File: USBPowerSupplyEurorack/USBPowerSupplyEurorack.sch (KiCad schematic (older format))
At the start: 9 parts, among them J1 1734366-1, T1 RS6-0512D

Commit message: changed diode for lower forward voltage, prepared 2HP PCB contour
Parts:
- removed D1: SS36, SS36:DIOM8059X265N, symbol SS36:SS36
- added C?: 100nF close to Switch, symbol Device:CP_Small
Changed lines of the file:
@@
 $EndDescr
-$Comp
-L SS36:SS36 D1
-U 1 1 5FE03083
-P 2330 1470
-F 0 "D1" H 2730 1203 50  0000 C CNN
-F 1 "SS36" H 2730 1294 50  0000 C CNN
-F 2 "SS36:DIOM8059X265N" H 2830 1620 50  0001 L CNN
-F 3 "http://www.onsemi.com/pub/Collateral/SS39-D.PDF" H 2830 1520 50  0001 L CNN
-F 4 "ON SEMICONDUCTOR - SS36 - DIODE, SCHOTTKY, 3A, 60V, DO-214AB-3" H 2830 1420 50  0001 L CNN "Description"
-F 5 "2.65" H 2830 1320 50  0001 L CNN "Height"
-F 6 "ON Semiconductor" H 2830 1220 50  0001 L CNN "Manufacturer_Name"
-F 7 "SS36" H 2830 1120 50  0001 L CNN "Manufacturer_Part_Number"
-F 8 "SS36" H 2830 1020 50  0001 L CNN "Arrow Part Number"
-F 9 "https://www.arrow.com/en/products/ss36/on-semiconductor" H 2830 920 50  0001 L CNN "Arrow Price/Stock"
-F 10 "512-SS36" H 2830 820 50  0001 L CNN "Mouser Part Number"
-F 11 "https://www.mouser.co.uk/ProductDetail/ON-Semiconductor-Fairchild/SS36/?qs=3wuez3jz59JyNj1can%252BtMw%3D%3D" H 2830 720 50  0001 L CNN "Mouser Price/Stock"
-	1    2330 1470
-	-1   0    0    1
-$EndComp
 $Comp
 L Device:CP1_Small C1
@@
 NoConn ~ 1510 1670
 $Comp
+L Device:CP1_Small C?
+U 1 1 5FE2664F
+P 6420 5130
+F 0 "C?" H 6511 5176 50  0000 L CNN
+F 1 "22uF" H 6511 5085 50  0000 L CNN
+F 2 "" H 6420 5130 50  0001 C CNN
+F 3 "~" H 6420 5130 50  0001 C CNN
+	1    6420 5130
+	1    0    0    -1
+$EndComp
+Wire Wire Line
+	6420 5230 6420 5420
+Wire Wire Line
+	6420 5030 6420 4840
+Wire Wire Line
+	6010 4970 6010 4840
+Wire Wire Line
+	6010 4840 6420 4840
+Connection ~ 6420 4840
+Wire Wire Line
+	6010 5270 6010 5420
+Wire Wire Line
+	6010 5420 6420 5420
+Connection ~ 6420 5420
+Wire Wire Line
+	5630 5020 5630 4840
+Wire Wire Line
+	5630 4840 6010 4840
+Connection ~ 6010 4840
+Wire Wire Line
+	5630 5220 5630 5420
+Wire Wire Line
+	5630 5420 6010 5420
+Connection ~ 6010 5420
+$Comp
+L power:GND #PWR?
+U 1 1 5FE34916
+P 5630 5520
+F 0 "#PWR?" H 5630 5270 50  0001 C CNN
+F 1 "GND" H 5635 5347 50  0000 C CNN
+F 2 "" H 5630 5520 50  0001 C CNN
+F 3 "" H 5630 5520 50  0001 C CNN
+	1    5630 5520
+	1    0    0    -1
+$EndComp
+Wire Wire Line
+	5630 5520 5630 5420
+Connection ~ 5630 5420
+Wire Wire Line
+	2230 1470 2310 1470
+Wire Wire Line
+	2310 1470 2310 1420
+Wire Wire Line
+	5630 4740 5630 4840
+Connection ~ 5630 4840
+Text GLabel 9120 4870 2    50   Input ~ 0
++Vin
+Text GLabel 9400 5180 2    50   Input ~ 0
+-Vin
+Wire Wire Line
+	6830 4840 6830 5090
+Wire Wire Line
+	6420 4840 6830 4840
+Wire Wire Line
+	6830 5420 6830 5190
+Wire Wire Line
+	6420 5420 6830 5420
+$Comp
 L 744235601:744235601 L?
 U 1 1 5FE25D51
@@
 $EndComp
 $Comp
-L Device:CP1_Small C?
-U 1 1 5FE2664F
-P 6420 5130
-F 0 "C?" H 6511 5176 50  0000 L CNN
-F 1 "22uF" H 6511 5085 50  0000 L CNN
-F 2 "" H 6420 5130 50  0001 C CNN
-F 3 "~" H 6420 5130 50  0001 C CNN
-	1    6420 5130
-	1    0    0    -1
-$EndComp
-Wire Wire Line
-	6420 5230 6420 5420
-Wire Wire Line
-	6420 5420 6830 5420
-Wire Wire Line
-	6830 5420 6830 5190
-Wire Wire Line
-	6420 5030 6420 4840
-Wire Wire Line
-	6420 4840 6830 4840
-Wire Wire Line
-	6830 4840 6830 5090
-Wire Wire Line
-	6010 4970 6010 4840
-Wire Wire Line
-	6010 4840 6420 4840
-Connection ~ 6420 4840
-Wire Wire Line
-	6010 5270 6010 5420
-Wire Wire Line
-	6010 5420 6420 5420
-Connection ~ 6420 5420
-Wire Wire Line
-	5630 5020 5630 4840
-Wire Wire Line
-	5630 4840 6010 4840
-Connection ~ 6010 4840
-Wire Wire Line
-	5630 5220 5630 5420
-Wire Wire Line
-	5630 5420 6010 5420
-Connection ~ 6010 5420
-$Comp
-L power:GND #PWR?
-U 1 1 5FE34916
-P 5630 5520
-F 0 "#PWR?" H 5630 5270 50  0001 C CNN
-F 1 "GND" H 5635 5347 50  0000 C CNN
-F 2 "" H 5630 5520 50  0001 C CNN
-F 3 "" H 5630 5520 50  0001 C CNN
-	1    5630 5520
-	1    0    0    -1
-$EndComp
-Wire Wire Line
-	5630 5520 5630 5420
-Connection ~ 5630 5420
-Text GLabel 7630 5190 2    50   Input ~ 0
--Vin
-Text GLabel 7630 5090 2    50   Input ~ 0
-+Vin
-Wire Wire Line
-	2230 1470 2310 1470
-Wire Wire Line
-	2310 1470 2310 1420
-Wire Wire Line
-	5630 4740 5630 4840
-Connection ~ 5630 4840
+L Device:CP_Small C?
+U 1 1 5FE49BEB
+P 8000 5130
+F 0 "C?" H 8088 5176 50  0000 L CNN
+F 1 "100nF close to Switch" H 8088 5085 50  0000 L CNN
+F 2 "" H 8000 5130 50  0001 C CNN
+F 3 "~" H 8000 5130 50  0001 C CNN
+	1    8000 5130
+	1    0    0    -1
+$EndComp
 $EndSCHEMATC

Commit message: completed schematics
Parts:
- added C4: 100nF MLCC, symbol Device:CP_Small
- added C5, C6: 1uF, symbol Device:CP1_Small
- added C7: 47uF, symbol Device:CP1_Small
- added D1: LSM115JE3_TR13, DIOM5436X330N, symbol LSM115JE3_TR13:LSM115JE3_TR13
- added D3, D4: 1N4004, Diode_THT:D_DO-41_SOD81_P10.16mm_Horizontal, symbol Diode:1N4004
- added J2: EURO_PWR_2x5, symbol eurocad:EURO_PWR_2x5
- C2: renamed from C?; value 22uF -> 22uFMLCC
- C3: renamed from C?; value 100nF close to Switch -> 100nF MLCC
- gave numbers to parts that had none: 2
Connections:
- net labels added: COM
- wire segments 26 -> 59
- no-connect marks 4 -> 5
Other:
- note added: "DC-DC switching regulator"
- note added: "Output connector"
- note added: "Output filtering"
- note added: "Pre-regulator filtering and surge protection"
- moved on the sheet: C1, C2, C3, D2, J1, L1, R1, S1

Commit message: finished schematics, added PMOS for reversed polarity protection
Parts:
- removed D1: LSM115JE3_TR13, DIOM5436X330N, symbol LSM115JE3_TR13:LSM115JE3_TR13
- added F1: 1812L110_16DR, FUSC4632X125N, symbol 1812L110_16DR:1812L110_16DR
- added Q1: Q_PMOS_GSD, digikey-footprints:SOT-23-3, symbol Device:Q_PMOS_GSD
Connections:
- wire segments 59 -> 66
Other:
- note added: "Pre-regulator filtering and surge/reversed polarity protection"
- note removed: "Pre-regulator filtering and surge protection"
- moved on the sheet: C1, C2, C3, C4, C5, C6, C7, D2, D3, D4, J1, J2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

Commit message: finished schematics
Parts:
- removed T1: RS6-0512D, RS6-0512D:RS60505S, symbol RS6-0512D:RS6-0512D
- added PS? (x2): RS6-0512S, RS6-0512S:RS60512S, symbol RS6-0512S:RS6-0512S
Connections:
- net labels added: +12, -12, 0V
- wire segments 66 -> 68
- no-connect marks 5 -> 8
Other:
- note added: "DC-DC switching regulators"
- note removed: "DC-DC switching regulator"
- moved on the sheet: C3, C4, C5, C6, D3, D4, J2

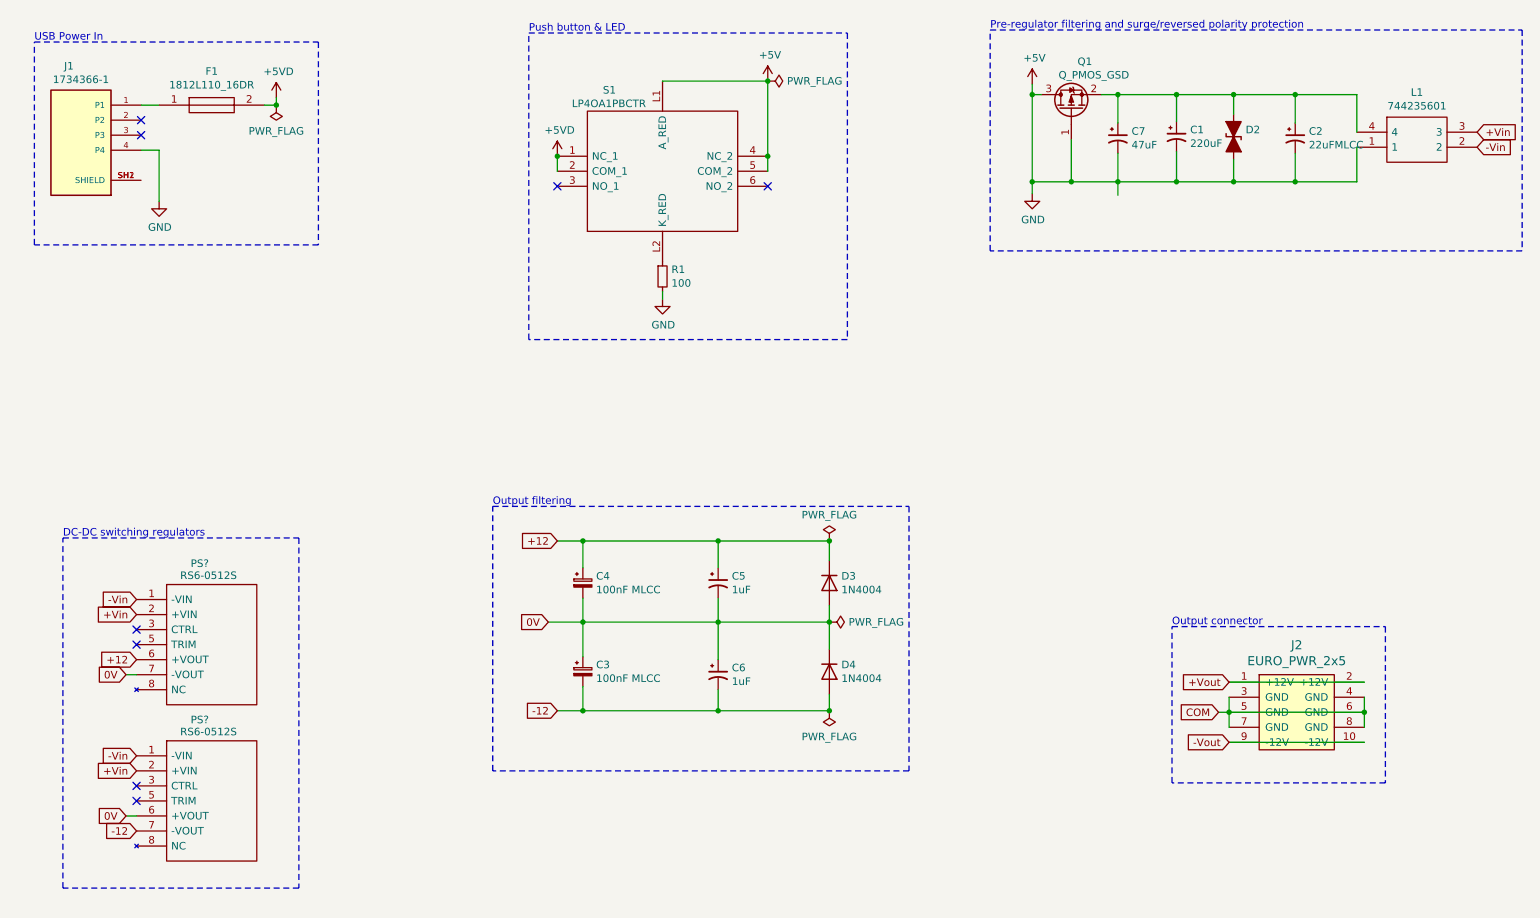
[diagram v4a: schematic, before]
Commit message: replaced power plug with open one
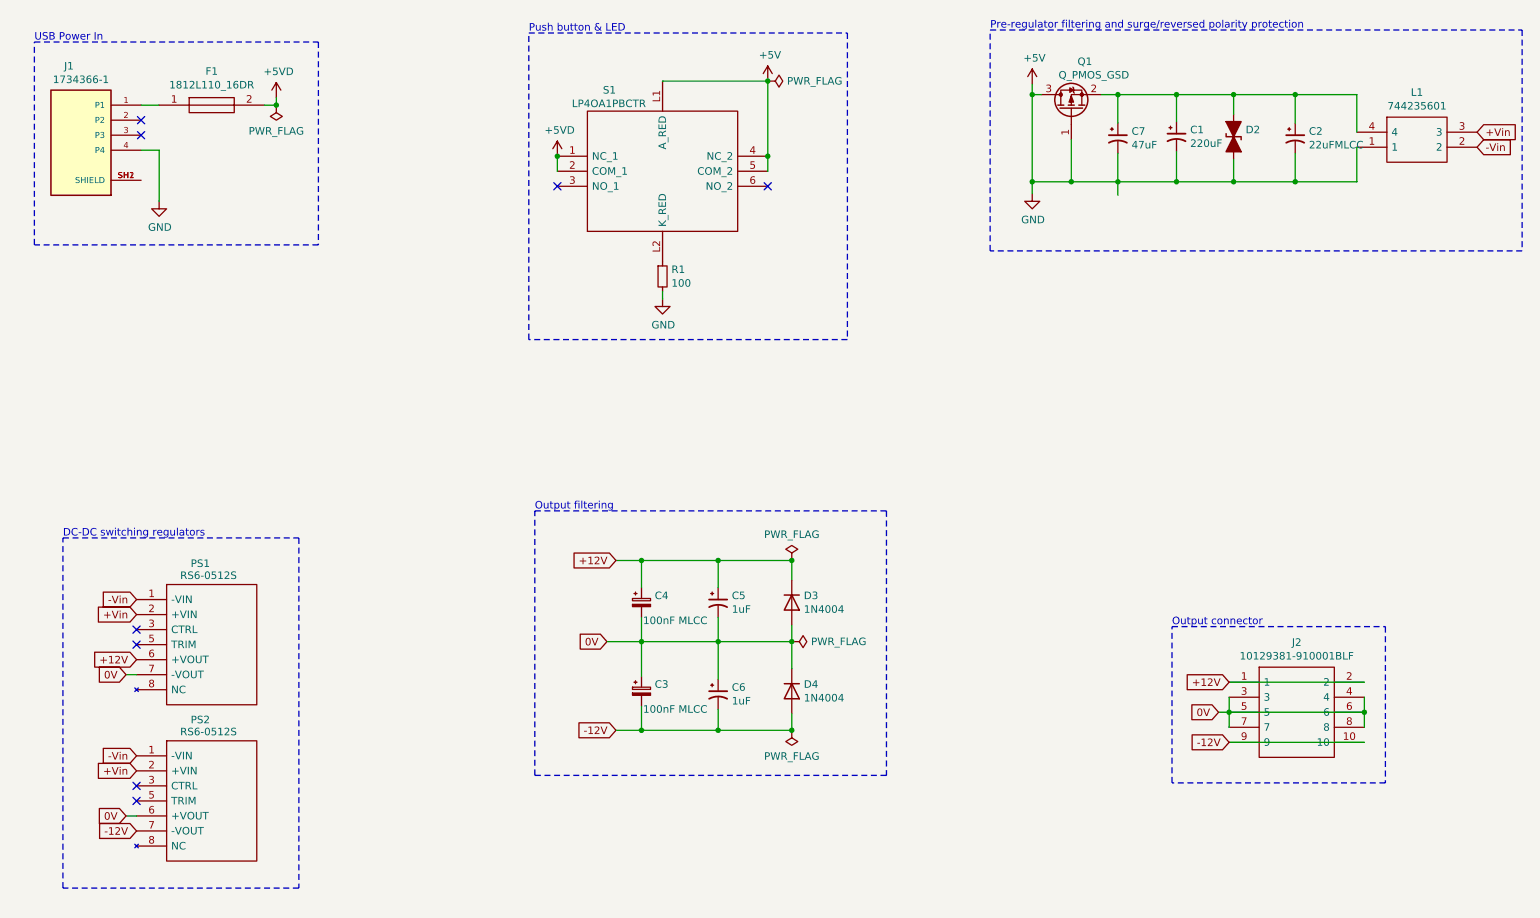
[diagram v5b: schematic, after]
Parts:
- removed J2: EURO_PWR_2x5, symbol eurocad:EURO_PWR_2x5
- added J2: 10129381-910001BLF, HDRV10W67P254_2X5_1270X483X858P, symbol 10129381-910001BLF:10129381-910001BLF
- gave numbers to parts that had none: 2
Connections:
- net 0V: now also J2.3, J2.4, J2.5, J2.6, J2.7, J2.8
- net +12 renamed +12V
- net +12V: now also J2.1, J2.2
- net -12 renamed -12V
- net -12V: now also J2.10, J2.9
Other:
- moved on the sheet: C3, C4, C5, C6, D3, D4
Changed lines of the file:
@@
 L Device:CP_Small C3
 U 1 1 5FE49BEB
-P 4600 5260
-F 0 "C3" H 4688 5306 50  0000 L CNN
-F 1 "100nF MLCC" H 4688 5215 50  0000 L CNN
-F 2 "" H 4600 5260 50  0001 C CNN
-F 3 "~" H 4600 5260 50  0001 C CNN
-	1    4600 5260
+P 4990 5390
+F 0 "C3" H 5078 5436 50  0000 L CNN
+F 1 "100nF MLCC" H 5000 5270 50  0000 L CNN
+F 2 "" H 4990 5390 50  0001 C CNN
+F 3 "~" H 4990 5390 50  0001 C CNN
+	1    4990 5390
 	1    0    0    -1
 $EndComp
@@
 $EndComp
 Wire Wire Line
-	4600 5360 4600 5520
-Wire Wire Line
-	4600 5520 4430 5520
+	4990 5490 4990 5650
+Wire Wire Line
+	4990 5650 4820 5650
 Wire Wire Line
 	8550 1420 8160 1420
@@
 L Diode:1N4004 D3
 U 1 1 5FE6DCB8
-P 6240 4670
-F 0 "D3" V 6194 4750 50  0000 L CNN
-F 1 "1N4004" V 6285 4750 50  0000 L CNN
-F 2 "Diode_THT:D_DO-41_SOD81_P10.16mm_Horizontal" H 6240 4495 50  0001 C CNN
-F 3 "http://www.vishay.com/docs/88503/1n4001.pdf" H 6240 4670 50  0001 C CNN
-	1    6240 4670
+P 5990 4800
+F 0 "D3" V 5944 4880 50  0000 L CNN
+F 1 "1N4004" V 6035 4880 50  0000 L CNN
+F 2 "Diode_THT:D_DO-41_SOD81_P10.16mm_Horizontal" H 5990 4625 50  0001 C CNN
+F 3 "http://www.vishay.com/docs/88503/1n4001.pdf" H 5990 4800 50  0001 C CNN
+	1    5990 4800
 	0    1    1    0
 $EndComp
@@
 L Device:CP_Small C4
 U 1 1 5FE6E630
-P 4600 4670
-F 0 "C4" H 4688 4716 50  0000 L CNN
-F 1 "100nF MLCC" H 4688 4625 50  0000 L CNN
-F 2 "" H 4600 4670 50  0001 C CNN
-F 3 "~" H 4600 4670 50  0001 C CNN
-	1    4600 4670
-	1    0    0    -1
-$EndComp
-Wire Wire Line
-	4430 4390 4600 4390
-Wire Wire Line
-	4600 4390 4600 4570
-Wire Wire Line
-	4600 4770 4600 4930
-Wire Wire Line
-	4600 4930 4370 4930
-Wire Wire Line
-	4600 5160 4600 4930
-Connection ~ 4600 4930
+P 4990 4800
+F 0 "C4" H 5078 4846 50  0000 L CNN
+F 1 "100nF MLCC" H 5000 4680 50  0000 L CNN
+F 2 "" H 4990 4800 50  0001 C CNN
+F 3 "~" H 4990 4800 50  0001 C CNN
+	1    4990 4800
+	1    0    0    -1
+$EndComp
+Wire Wire Line
+	4820 4520 4990 4520
+Wire Wire Line
+	4990 4520 4990 4700
+Wire Wire Line
+	4990 4900 4990 5060
+Wire Wire Line
+	4990 5060 4760 5060
+Wire Wire Line
+	4990 5290 4990 5060
+Connection ~ 4990 5060
 $Comp
 L Device:CP1_Small C5
 U 1 1 5FE73D6E
-P 5500 4670
-F 0 "C5" H 5591 4716 50  0000 L CNN
-F 1 "1uF" H 5591 4625 50  0000 L CNN
-F 2 "" H 5500 4670 50  0001 C CNN
-F 3 "~" H 5500 4670 50  0001 C CNN
-	1    5500 4670
+P 5500 4800
+F 0 "C5" H 5591 4846 50  0000 L CNN
+F 1 "1uF" H 5591 4755 50  0000 L CNN
+F 2 "" H 5500 4800 50  0001 C CNN
+F 3 "~" H 5500 4800 50  0001 C CNN
+	1    5500 4800
 	1    0    0    -1
 $EndComp
@@
 L Device:CP1_Small C6
 U 1 1 5FE74A1F
-P 5500 5280
-F 0 "C6" H 5591 5326 50  0000 L CNN
-F 1 "1uF" H 5591 5235 50  0000 L CNN
-F 2 "" H 5500 5280 50  0001 C CNN
-F 3 "~" H 5500 5280 50  0001 C CNN
-	1    5500 5280
-	1    0    0    -1
-$EndComp
-Wire Wire Line
-	4600 4390 5500 4390
-Wire Wire Line
-	5500 4390 5500 4570
-Connection ~ 4600 4390
-Wire Wire Line
-	5500 4770 5500 4930
-Wire Wire Line
-	5500 5380 5500 5520
-Wire Wire Line
-	5500 5520 4600 5520
-Connection ~ 4600 5520
-Wire Wire Line
-	4600 4930 5500 4930
-Connection ~ 5500 4930
-Wire Wire Line
-	5500 4930 5500 5180
+P 5500 5410
+F 0 "C6" H 5591 5456 50  0000 L CNN
+F 1 "1uF" H 5591 5365 50  0000 L CNN
+F 2 "" H 5500 5410 50  0001 C CNN
+F 3 "~" H 5500 5410 50  0001 C CNN
+	1    5500 5410
+	1    0    0    -1
+$EndComp
+Wire Wire Line
+	4990 4520 5500 4520
+Wire Wire Line
+	5500 4520 5500 4700
+Connection ~ 4990 4520
+Wire Wire Line
+	5500 4900 5500 5060
+Wire Wire Line
+	5500 5510 5500 5650
+Wire Wire Line
+	5500 5650 4990 5650
+Connection ~ 4990 5650
+Wire Wire Line
+	4990 5060 5500 5060
+Connection ~ 5500 5060
+Wire Wire Line
+	5500 5060 5500 5310
 $Comp
 L Diode:1N4004 D4
 U 1 1 5FE81B4A
-P 6240 5260
-F 0 "D4" V 6194 5340 50  0000 L CNN
-F 1 "1N4004" V 6285 5340 50  0000 L CNN
-F 2 "Diode_THT:D_DO-41_SOD81_P10.16mm_Horizontal" H 6240 5085 50  0001 C CNN
-F 3 "http://www.vishay.com/docs/88503/1n4001.pdf" H 6240 5260 50  0001 C CNN
-	1    6240 5260
+P 5990 5390
+F 0 "D4" V 5944 5470 50  0000 L CNN
+F 1 "1N4004" V 6035 5470 50  0000 L CNN
+F 2 "Diode_THT:D_DO-41_SOD81_P10.16mm_Horizontal" H 5990 5215 50  0001 C CNN
+F 3 "http://www.vishay.com/docs/88503/1n4001.pdf" H 5990 5390 50  0001 C CNN
+	1    5990 5390
 	0    1    1    0
 $EndComp
 Wire Wire Line
-	5500 5520 6240 5520
-Wire Wire Line
-	6240 5520 6240 5410
-Connection ~ 5500 5520
-Wire Wire Line
-	5500 4930 6240 4930
-Wire Wire Line
-	6240 4820 6240 4930
-Connection ~ 6240 4930
-Wire Wire Line
-	6240 4930 6240 5110
-Wire Wire Line
-	6240 4520 6240 4390
-Wire Wire Line
-	6240 4390 5500 4390
-Connection ~ 5500 4390
+	5500 5650 5990 5650
+Wire Wire Line
+	5990 5650 5990 5540
+Connection ~ 5500 5650
+Wire Wire Line
+	5500 5060 5990 5060
+Wire Wire Line
+	5990 4950 5990 5060
+Connection ~ 5990 5060
+Wire Wire Line
+	5990 5060 5990 5240
+Wire Wire Line
+	5990 4650 5990 4520
+Wire Wire Line
+	5990 4520 5500 4520
+Connection ~ 5500 4520
 Wire Notes Line
 	1140 4370 2710 4370
@@
 Text Notes 1140 4370 0    50   ~ 0
 DC-DC switching regulators
-$Comp
-L eurocad:EURO_PWR_2x5 J2
-U 1 1 5FE9238E
-P 9350 5530
-F 0 "J2" H 9350 5977 60  0000 C CNN
-F 1 "EURO_PWR_2x5" H 9350 5871 60  0000 C CNN
-F 2 "" H 9350 5530 60  0000 C CNN
-F 3 "" H 9350 5530 60  0000 C CNN
-	1    9350 5530
-	1    0    0    -1
-$EndComp
-Wire Notes Line
-	4000 4160 6770 4160
-Wire Notes Line
-	6770 4160 6770 5920
-Wire Notes Line
-	6770 5920 4000 5920
-Wire Notes Line
-	4000 5920 4000 4160
-Text Notes 4000 4160 0    50   ~ 0
+Wire Notes Line
+	4280 4190 6620 4190
+Wire Notes Line
+	6620 4190 6620 5950
+Wire Notes Line
+	6620 5950 4280 5950
+Wire Notes Line
+	4280 5950 4280 4190
+Text Notes 4280 4190 0    50   ~ 0
 Output filtering
 Text GLabel 8900 5330 0    50   Input ~ 0
-+Vout
++12V
 Text GLabel 8830 5530 0    50   Input ~ 0
-COM
+0V
 Text GLabel 8900 5730 0    50   Input ~ 0
--Vout
+-12V
 Wire Wire Line
 	8900 5430 8900 5530
@@
 L power:PWR_FLAG #FLG0101
 U 1 1 5FEBA228
-P 6240 4390
-F 0 "#FLG0101" H 6240 4465 50  0001 C CNN
-F 1 "PWR_FLAG" H 6240 4563 50  0000 C CNN
-F 2 "" H 6240 4390 50  0001 C CNN
-F 3 "~" H 6240 4390 50  0001 C CNN
-	1    6240 4390
-	1    0    0    -1
-$EndComp
-Connection ~ 6240 4390
+P 5990 4520
+F 0 "#FLG0101" H 5990 4595 50  0001 C CNN
+F 1 "PWR_FLAG" H 5990 4693 50  0000 C CNN
+F 2 "" H 5990 4520 50  0001 C CNN
+F 3 "~" H 5990 4520 50  0001 C CNN
+	1    5990 4520
+	1    0    0    -1
+$EndComp
+Connection ~ 5990 4520
 $Comp
 L power:PWR_FLAG #FLG0103
 U 1 1 5FEBB245
-P 6240 5520
-F 0 "#FLG0103" H 6240 5595 50  0001 C CNN
-F 1 "PWR_FLAG" H 6240 5693 50  0000 C CNN
-F 2 "" H 6240 5520 50  0001 C CNN
-F 3 "~" H 6240 5520 50  0001 C CNN
-	1    6240 5520
+P 5990 5650
+F 0 "#FLG0103" H 5990 5725 50  0001 C CNN
+F 1 "PWR_FLAG" H 5990 5823 50  0000 C CNN
+F 2 "" H 5990 5650 50  0001 C CNN
+F 3 "~" H 5990 5650 50  0001 C CNN
+	1    5990 5650
 	-1   0    0    1
 $EndComp
-Connection ~ 6240 5520
+Connection ~ 5990 5650
 $Comp
 L power:PWR_FLAG #FLG0104
@@
 L power:PWR_FLAG #FLG0102
 U 1 1 5FEBAD77
-P 6240 4930
-F 0 "#FLG0102" H 6240 5005 50  0001 C CNN
-F 1 "PWR_FLAG" V 6240 5058 50  0000 L CNN
-F 2 "" H 6240 4930 50  0001 C CNN
-F 3 "~" H 6240 4930 50  0001 C CNN
-	1    6240 4930
+P 5990 5060
+F 0 "#FLG0102" H 5990 5135 50  0001 C CNN
+F 1 "PWR_FLAG" V 5990 5188 50  0000 L CNN
+F 2 "" H 5990 5060 50  0001 C CNN
+F 3 "~" H 5990 5060 50  0001 C CNN
+	1    5990 5060
 	0    1    1    0
 $EndComp
 $Comp
-L RS6-0512S:RS6-0512S PS?
+L RS6-0512S:RS6-0512S PS1
 U 1 1 5FE5CD2D
 P 1630 4780
-F 0 "PS?" H 1990 5020 50  0000 L CNN
+F 0 "PS1" H 1990 5020 50  0000 L CNN
 F 1 "RS6-0512S" H 1920 4940 50  0000 L CNN
 F 2 "RS6-0512S:RS60512S" H 2480 4880 50  0001 L CNN
@@
 0V
 Text GLabel 1630 5180 0    50   Input ~ 0
-+12
++12V
 NoConn ~ 1630 5080
 Wire Wire Line
 	1560 5280 1630 5280
 $Comp
-L RS6-0512S:RS6-0512S PS?
+L RS6-0512S:RS6-0512S PS2
 U 1 1 5FE68DDD
 P 1630 5820
-F 0 "PS?" H 1990 6060 50  0000 L CNN
+F 0 "PS2" H 1990 6060 50  0000 L CNN
 F 1 "RS6-0512S" H 1920 5980 50  0000 L CNN
 F 2 "RS6-0512S:RS60512S" H 2480 5920 50  0001 L CNN
@@
 	1560 6220 1630 6220
 Text GLabel 1630 6320 0    50   Input ~ 0
--12
-Text GLabel 4430 5520 0    50   Input ~ 0
--12
-Text GLabel 4370 4930 0    50   Input ~ 0
+-12V
+Text GLabel 4820 5650 0    50   Input ~ 0
+-12V
+Text GLabel 4760 5060 0    50   Input ~ 0
 0V
-Text GLabel 4430 4390 0    50   Input ~ 0
-+12
+Text GLabel 4820 4520 0    50   Input ~ 0
++12V
+$Comp
+L 10129381-910001BLF:10129381-910001BLF J2
+U 1 1 5FE8C505
+P 8900 5330
+F 0 "J2" H 9350 5595 50  0000 C CNN
+F 1 "10129381-910001BLF" H 9350 5504 50  0000 C CNN
+F 2 "HDRV10W67P254_2X5_1270X483X858P" H 9650 5430 50  0001 L CNN
+F 3 "https://cdn.amphenol-icc.com/media/wysiwyg/files/drawing/10129381.pdf" H 9650 5330 50  0001 L CNN
+F 4 "EconoStik , Board to Board connector, Unshrouded Vertical Header, Through Hole, Double Row, 10 Positions, 2.54 mm (0.100in) Pitch" H 9650 5230 50  0001 L CNN "Description"
+F 5 "8.58" H 9650 5130 50  0001 L CNN "Height"
+F 6 "Amphenol" H 9650 5030 50  0001 L CNN "Manufacturer_Name"
+F 7 "10129381-910001BLF" H 9650 4930 50  0001 L CNN "Manufacturer_Part_Number"
+F 8 "649-1012938191001BLF" H 9650 4830 50  0001 L CNN "Mouser Part Number"
+F 9 "https://www.mouser.co.uk/ProductDetail/Amphenol-FCI/10129381-910001BLF?qs=0lQeLiL1qyYhmE%2FYsfo%2FnQ%3D%3D" H 9650 4730 50  0001 L CNN "Mouser Price/Stock"
+F 10 "10129381-910001BLF" H 9650 4630 50  0001 L CNN "Arrow Part Number"
+F 11 "https://www.arrow.com/en/products/10129381-910001blf/amphenol-fci" H 9650 4530 50  0001 L CNN "Arrow Price/Stock"
+	1    8900 5330
+	1    0    0    -1
+$EndComp
 $EndSCHEMATC
